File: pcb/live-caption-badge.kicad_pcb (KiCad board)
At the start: 2 copper layers, 170 x 100 mm, 75 parts, among them J1 Conn_01x09, J2 Conn_01x04_Socket, J3 Conn_01x09, J4 AudioJack4, J5 USB_C_Receptacle_USB2.0_16P, J6 Conn_01x06, J7 Conn_01x03, J8 Conn_01x03, J9 Conn_01x04, SW1 SW_DPDT_x2, SW2 RST, SW3 BTN, SW4 BTN, SW5 BTN, U1 ESP32-S3-WROOM-1, U2 HE9073A33M5R, U3 HE9073A33M5R, U4 ES7210, U5 ES8311, U6 IS31AP2005

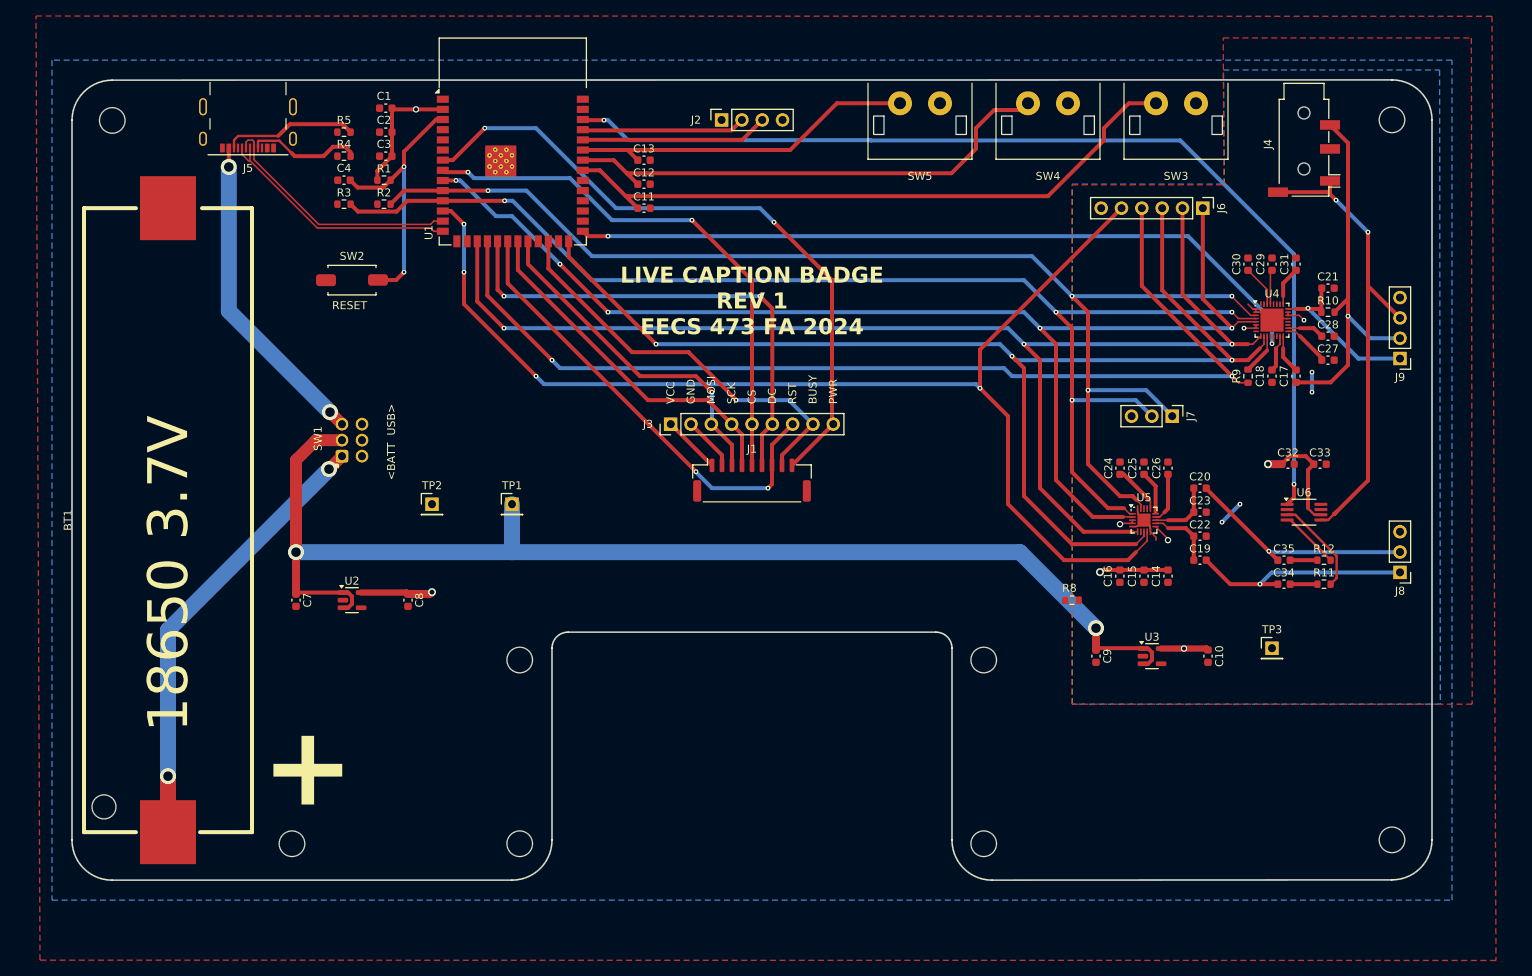
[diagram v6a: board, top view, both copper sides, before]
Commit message: pcb: Convert to 4-layer board
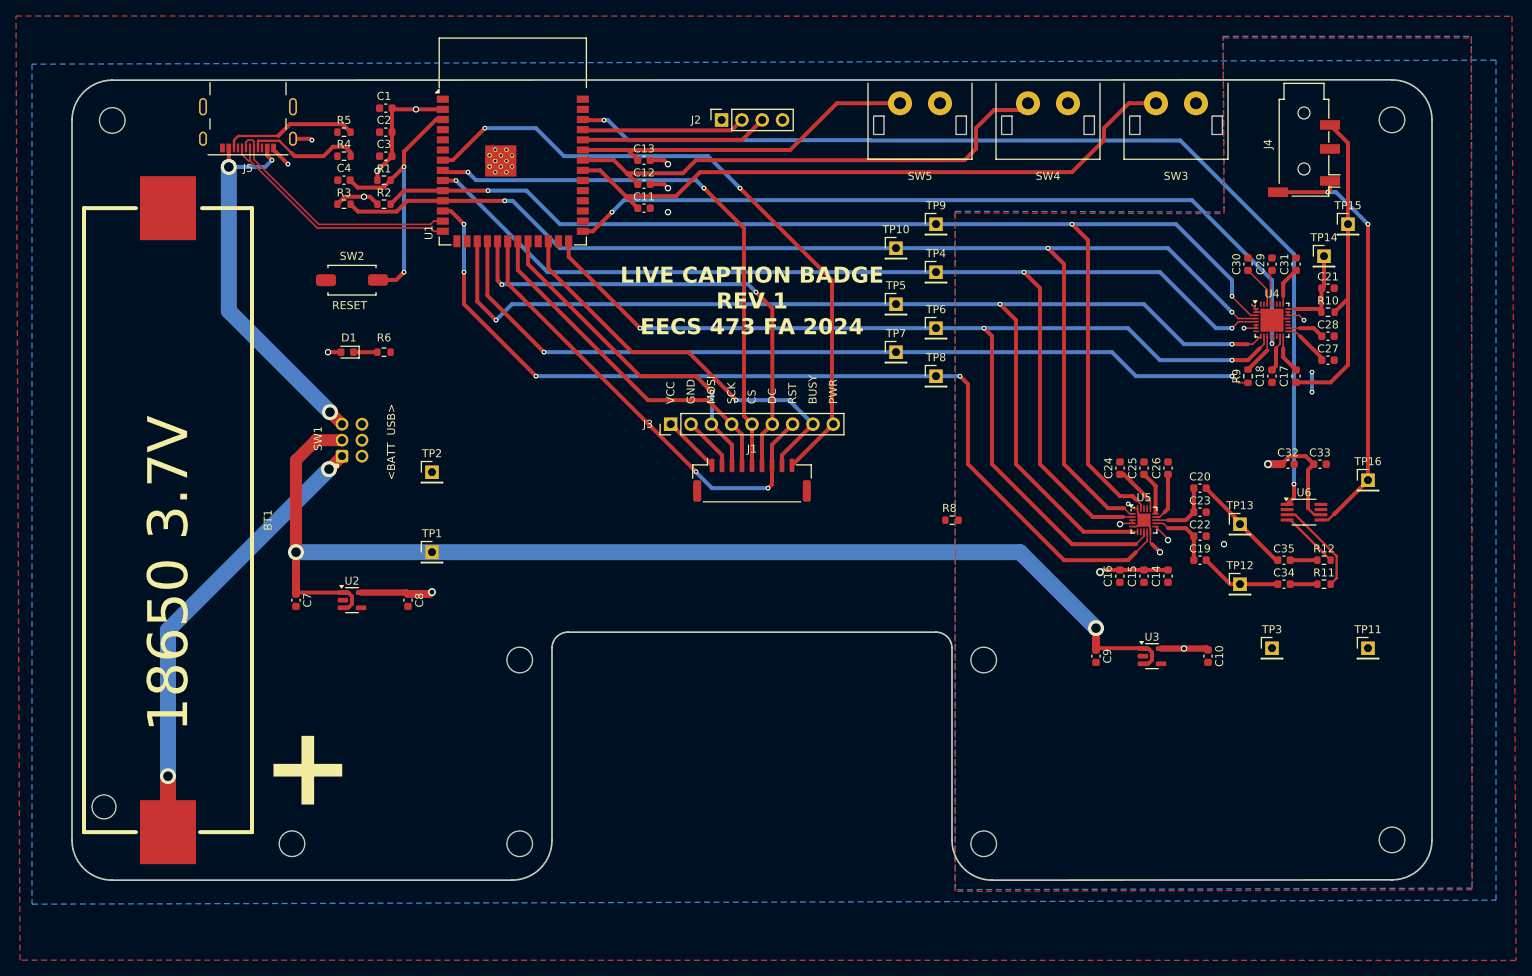
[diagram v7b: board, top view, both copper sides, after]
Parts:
- removed J6: Conn_01x06, Connector_PinHeader_2.54mm:PinHeader_1x06_P2.54mm_Vertical
- removed J7, J8: Conn_01x03, Connector_PinHeader_2.54mm:PinHeader_1x03_P2.54mm_Vertical
- removed J9: Conn_01x04, Connector_PinHeader_2.54mm:PinHeader_1x04_P2.54mm_Vertical
- added D1: LED, LED_SMD:LED_0603_1608Metric, F.Cu at (64.4, 64.0)
- added R6: 1k, Resistor_SMD:R_0603_1608Metric, F.Cu at (69.0, 64.0)
- added TP10: TestPoint, Connector_PinHeader_2.54mm:PinHeader_1x01_P2.54mm_Vertical, F.Cu at (133.0, 51.0)
- added TP11: TestPoint, Connector_PinHeader_2.54mm:PinHeader_1x01_P2.54mm_Vertical, F.Cu at (192.0, 101.0)
- added TP12: TestPoint, Connector_PinHeader_2.54mm:PinHeader_1x01_P2.54mm_Vertical, F.Cu at (176.0, 93.0)
- added TP13: TestPoint, Connector_PinHeader_2.54mm:PinHeader_1x01_P2.54mm_Vertical, F.Cu at (176.0, 85.5)
- added TP14: TestPoint, Connector_PinHeader_2.54mm:PinHeader_1x01_P2.54mm_Vertical, F.Cu at (186.5, 52.0)
- added TP15: TestPoint, Connector_PinHeader_2.54mm:PinHeader_1x01_P2.54mm_Vertical, F.Cu at (189.5, 48.0)
- added TP16: TestPoint, Connector_PinHeader_2.54mm:PinHeader_1x01_P2.54mm_Vertical, F.Cu at (192.0, 80.0)
- added TP4: TestPoint, Connector_PinHeader_2.54mm:PinHeader_1x01_P2.54mm_Vertical, F.Cu at (138.0, 54.0)
- added TP5: TestPoint, Connector_PinHeader_2.54mm:PinHeader_1x01_P2.54mm_Vertical, F.Cu at (133.0, 58.0)
- added TP6: TestPoint, Connector_PinHeader_2.54mm:PinHeader_1x01_P2.54mm_Vertical, F.Cu at (138.0, 61.0)
- added TP7: TestPoint, Connector_PinHeader_2.54mm:PinHeader_1x01_P2.54mm_Vertical, F.Cu at (133.0, 64.0)
- added TP8: TestPoint, Connector_PinHeader_2.54mm:PinHeader_1x01_P2.54mm_Vertical, F.Cu at (138.0, 67.0)
- added TP9: TestPoint, Connector_PinHeader_2.54mm:PinHeader_1x01_P2.54mm_Vertical, F.Cu at (138.0, 48.0)
- U1: footprint RF_Module:ESP32-S3-WROOM-1 -> live-caption-badge:ESP32-S3-WROOM-1-LargerVias
- moved R8 18.0 mm to (140.0, 85.0)
- moved TP1 11.7 mm to (75.0, 89.0)
- moved TP2 4.00 mm to (75.0, 79.0)
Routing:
- net /I2S_SDIN: track 150.4 -> 120.0 mm
- net /I2S_SDOUT: track 132.0 -> 106.4 mm
- net /Audio/DAC_OUTP: track 28.3 -> 10.2 mm, vias 1 -> 0
- net /I2S_LRCK: track 155.2 -> 137.6 mm
- net /Audio/DAC_OUTN: track 29.1 -> 12.6 mm, vias 1 -> 0
- net /I2S_SCLK: track 160.9 -> 149.3 mm
- net GND: track 6.75 -> 16.8 mm, vias 0 -> 5
- net /Audio/MIC_BIAS: track 21.4 -> 11.4 mm, vias 1 -> 0
- net /I2S_MCLK: track 157.4 -> 148.7 mm, vias 5 -> 3
- net /Audio/MIC_IN: track 48.3 -> 40.7 mm, vias 1 -> 0
- net VBUS: track 40.4 -> 47.9 mm, vias 2 -> 3
- net +3V3: track 32.3 -> 39.6 mm, vias 2 -> 5
- net /ADC_INT: track 94.7 -> 100.9 mm
- net V_UNREG: track 155.0 -> 149.0 mm
- net /Audio/AUDIO_OUT: track 60.5 -> 55.4 mm
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- added copper zone on In1.Cu, net +3.3VA
- added copper zone on In1.Cu, net +3V3
- added copper zone on In2.Cu, net GND
- added copper zone on In2.Cu, net GNDA
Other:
- copper layers 2 -> 4

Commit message: pcb: it may or may not work
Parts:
- added C5: 1uF, Capacitor_SMD:C_0603_1608Metric, F.Cu at (74.0, 69.0)
- added R13: 0, Resistor_SMD:R_0603_1608Metric, F.Cu at (69.0, 49.0)
- added R14: 0, Resistor_SMD:R_0603_1608Metric, F.Cu at (69.0, 51.5)
- added REF**: MountingHole_3mm, MountingHole:MountingHole_3mm, F.Cu at (164.0, 70.0)
- added REF**: MountingHole_3mm, MountingHole:MountingHole_3mm, F.Cu at (35.0, 110.0)
- added REF**: MountingHole_3mm, MountingHole:MountingHole_3mm, F.Cu at (164.0, 116.5)
- added REF**: MountingHole_3mm, MountingHole:MountingHole_3mm, F.Cu at (144.0, 116.5)
- added REF**: MountingHole_3mm, MountingHole:MountingHole_3mm, F.Cu at (95.0, 88.0)
- added REF**: MountingHole_3mm, MountingHole:MountingHole_3mm, F.Cu at (86.0, 116.5)
- added REF**: MountingHole_3mm, MountingHole:MountingHole_3mm, F.Cu at (123.5, 34.0)
- added REF**: MountingHole_3mm, MountingHole:MountingHole_3mm, F.Cu at (42.0, 35.0)
- added REF**: MountingHole_3mm, MountingHole:MountingHole_3mm, F.Cu at (195.0, 116.5)
- added REF**: MountingHole_3mm, MountingHole:MountingHole_3mm, F.Cu at (135.0, 88.0)
- added REF**: MountingHole_3mm, MountingHole:MountingHole_3mm, F.Cu at (195.0, 70.0)
- added REF**: MountingHole_3mm, MountingHole:MountingHole_3mm, F.Cu at (195.0, 43.0)
- added SW6: RST, live-caption-badge:SW_Push_6x3mm, F.Cu at (65.0, 69.0)
- J1: footprint Connector_Molex:Molex_CLIK-Mate_502386-0970_1x09-1MP_P1.25mm_Horizontal -> live-caption-badge:Molex_CLIK-Mate_502386-0970_1x09-1MP_P1.25mm_Horizontal
- J2: value Conn_01x04_Socket -> Conn_01x06; footprint Connector_PinSocket_2.54mm:PinSocket_1x04_P2.54mm_Vertical -> Connector_PinHeader_2.54mm:PinHeader_1x06_P2.54mm_Vertical
- moved D1 27.0 mm to (64.4, 91.0)
- moved R6 27.0 mm to (69.0, 91.0)
- moved R8 10.0 mm to (140.0, 95.0)
- moved C7 6.00 mm to (58.0, 101.0)
- moved C8 6.00 mm to (72.0, 101.0)
- moved SW1 6.00 mm to (63.8, 83.0)
- moved TP1 6.00 mm to (75.0, 95.0)
- moved TP2 6.00 mm to (75.0, 85.0)
- moved U2 6.00 mm to (65.0, 101.0)
- moved J2 5.57 mm to (105.7, 34.5)
- moved SW2 5.00 mm to (65.0, 60.0)
- moved TP15 0.50 mm to (189.5, 47.5)
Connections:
- C4 pad 1: Net-(U1-EN) -> /ESP_EN
- J2 pad 4: GND -> /ESP_IO0
- R1 pad 2: Net-(U1-EN) -> /ESP_EN
- SW2 pad 2: Net-(U1-EN) -> /ESP_EN
- U1 pad 13: /USB_D- -> /ESP_D-
- U1 pad 14: /USB_D+ -> /ESP_D+
- U1 pad 27: /ADC_INT -> /ESP_IO0
- U1 pad 3: Net-(U1-EN) -> /ESP_EN
- U1 pad 31: unconnected-(U1-IO38-Pad31) -> /ADC_INT
- U4 pad 8: (no net) -> GNDA
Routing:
- net /ESP_IO0: track 0.00 -> 80.7 mm, vias 0 -> 3
- net /ESP_EN: track 0.00 -> 79.2 mm, vias 0 -> 3
- net Net-(U1-EN): track 33.4 -> 0.00 mm, vias 2 -> 0
- net /ESP_D+: track 0.00 -> 7.95 mm
- net /ESP_D-: track 0.00 -> 7.09 mm
- net /USB_D-: track 31.3 -> 24.2 mm
- net /USB_D+: track 31.5 -> 24.4 mm
- net VBUS: track 47.9 -> 54.1 mm
- net +BATT: track 56.0 -> 50.2 mm
- net /UART_RX: track 23.5 -> 18.1 mm
- net /UART_TX: track 20.3 -> 15.0 mm
- net /I2S_SDIN: track 120.0 -> 125.0 mm
- net V_UNREG: track 149.0 -> 146.5 mm
- net /I2S_LRCK: track 137.6 -> 139.9 mm
- net /I2S_SCLK: track 149.3 -> 151.3 mm
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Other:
- board text added: "3V3"
- board text added: "3V3A"
- board text added: "AUDIO_OUT"
- board text added: "EN"
- board text added: "ES7210 ADC"
- board text added: "ES8311 DAC"
- board text added: "FLASH"
- board text added: "GNDA"
- board text added: "I2C"
- board text added: "I2S"
- board text added: "IO0"
- board text added: "IS31AP2005 Amp"
- board text added: "LRCK"
- board text added: "MCLK"
- board text added: "MIC_BIAS"
- board text added: "MIC_IN"
- board text added: "OUTN"
- board text added: "OUTP"
- board text added: "RX"
- board text added: "SCL"
- board text added: "SCLK"
- board text added: "SDA"
- board text added: "SDIN DAC 8311"
- board text added: "SDOUT ADC 7210"
- board text added: "TX"
- board text added: "V_UNREG"
- board text added: "hey put it back!"
